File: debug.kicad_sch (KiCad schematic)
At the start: 47 parts, among them J701 USB4105-GF-A, J702 Conn_02x10_Odd_Even, U701 USBLC6-2SC6, U702 FT231XQ-R, U703 TCA9554PW

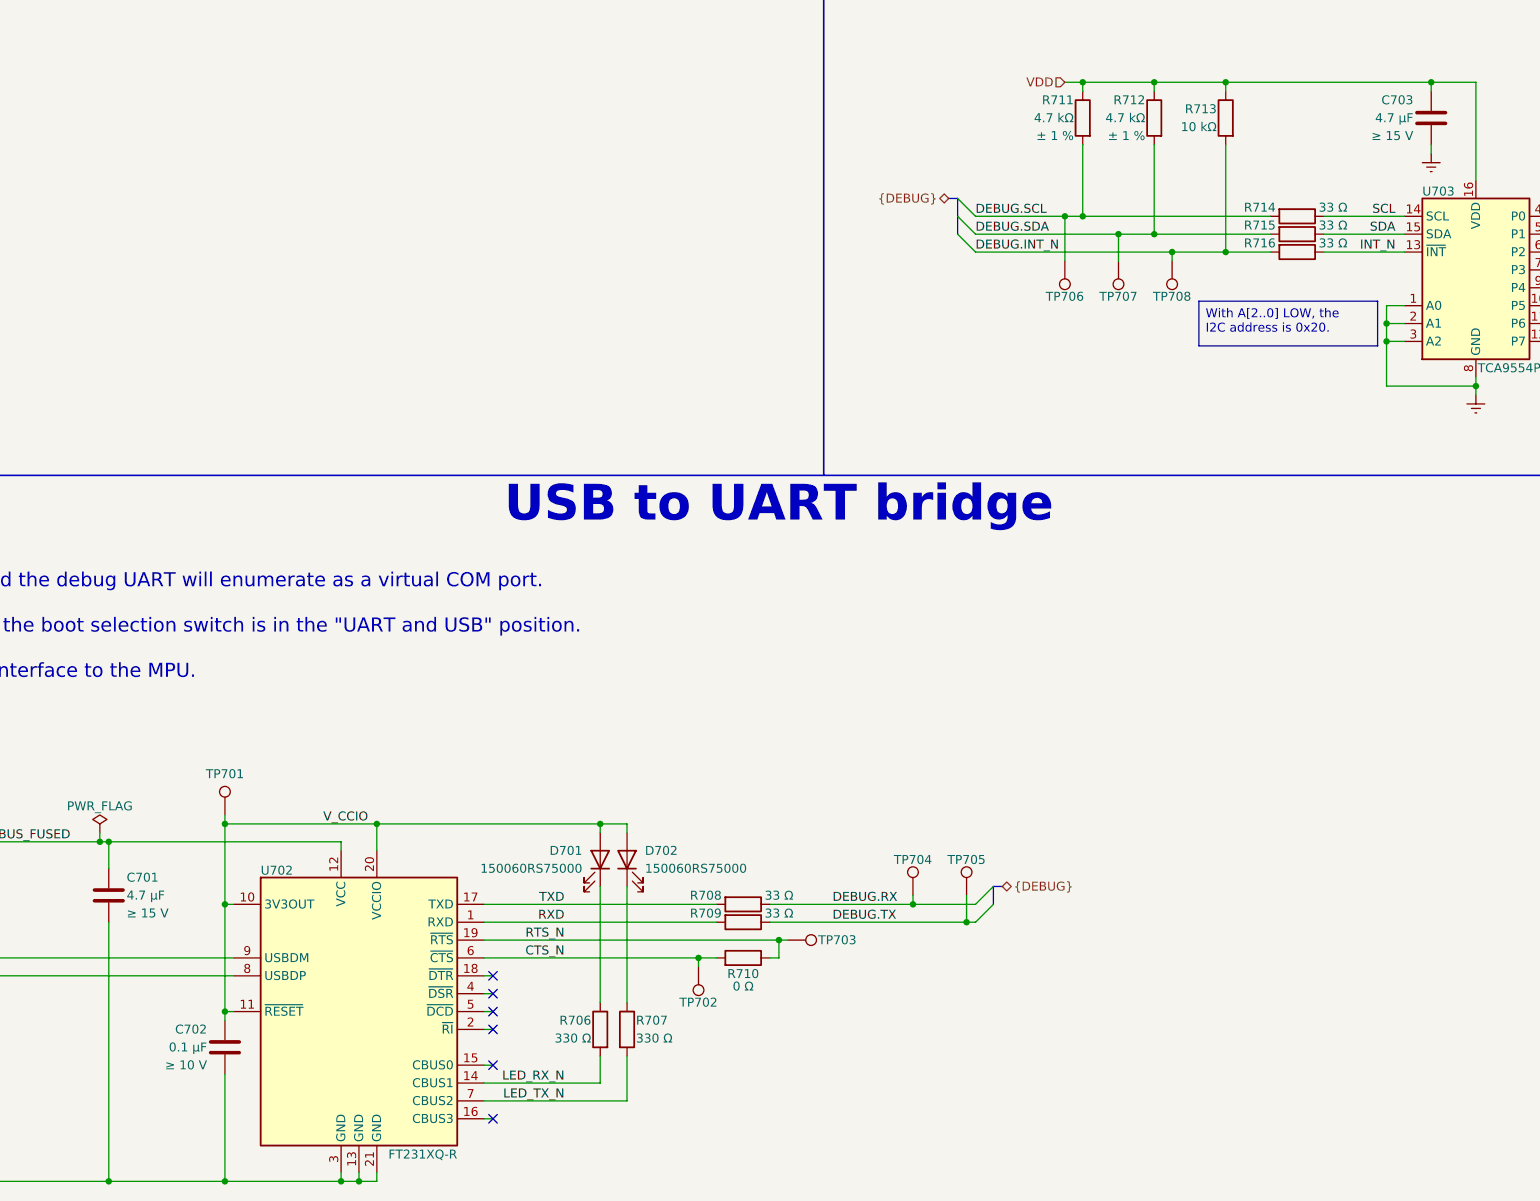
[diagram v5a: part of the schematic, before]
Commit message: Fix component values
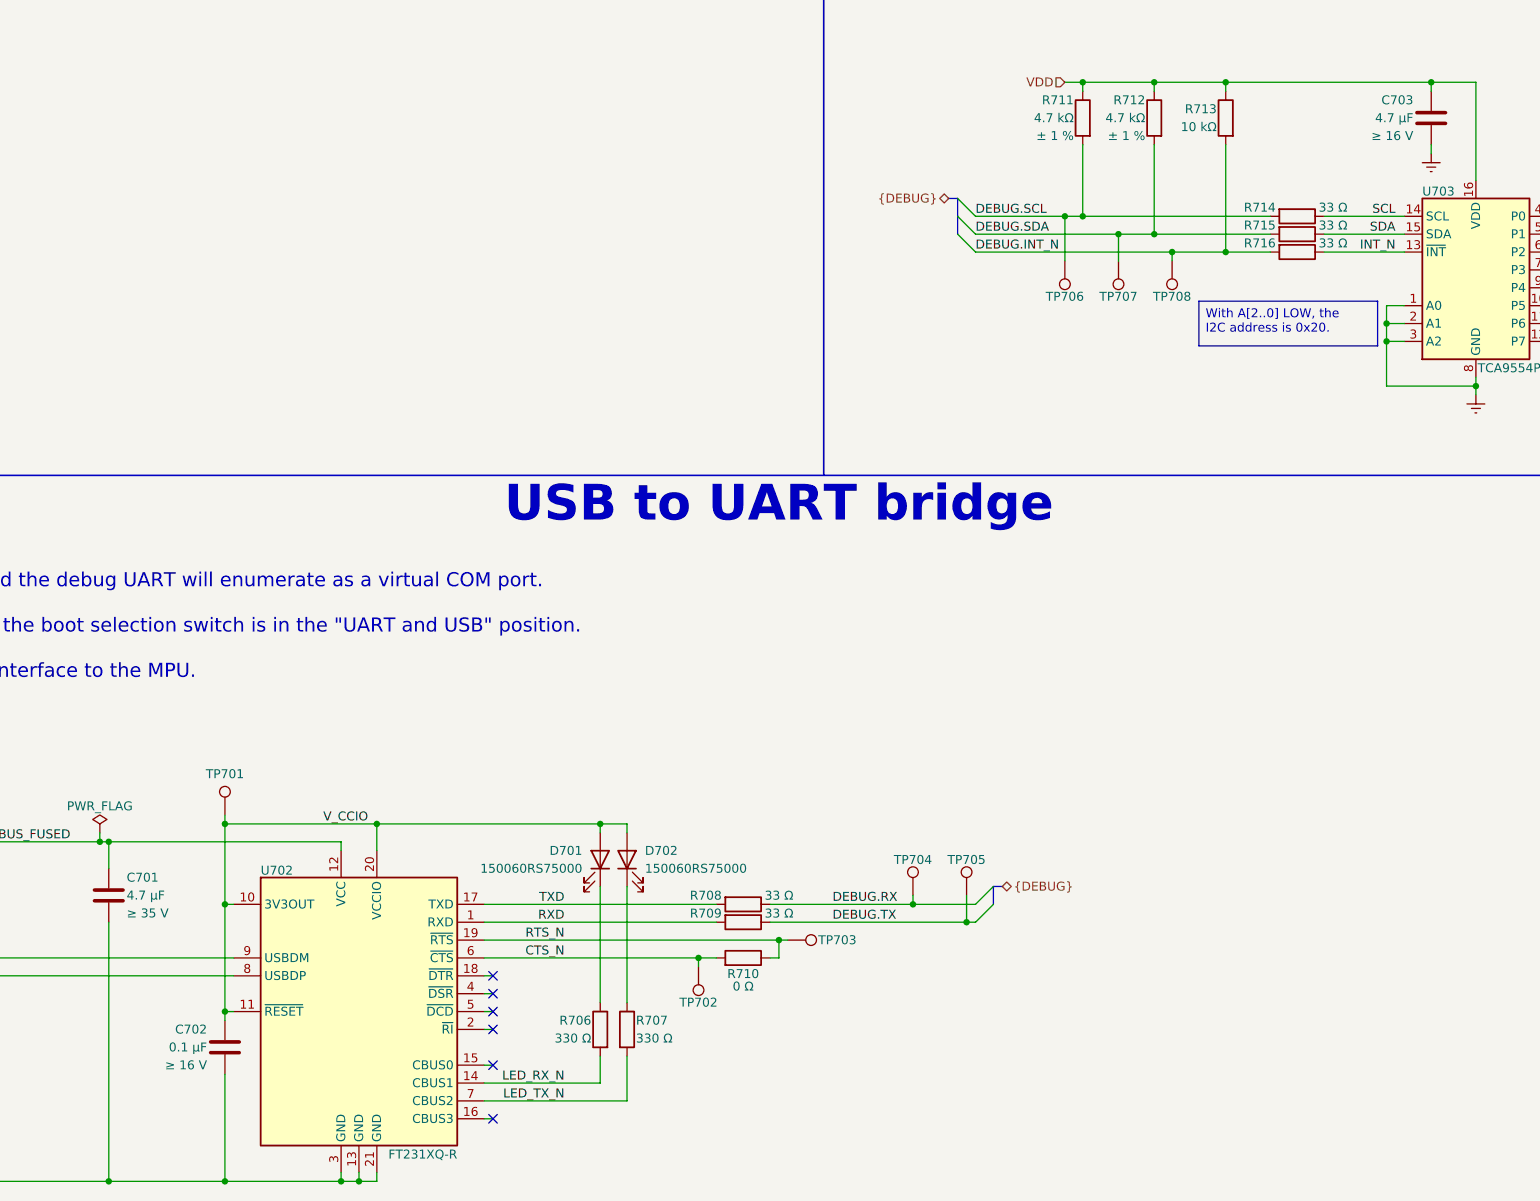
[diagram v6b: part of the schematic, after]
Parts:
- C701: Voltage rating ≥ 15 V -> ≥ 35 V
- C702: Voltage rating ≥ 10 V -> ≥ 16 V
- C703: Voltage rating ≥ 15 V -> ≥ 16 V
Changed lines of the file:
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@@
 			)
 		)
-		(property "Voltage rating" "≥ 15 V"
+		(property "Voltage rating" "≥ 16 V"
 			(at 299.72 88.9001 0)
 			(effects
@@
 			)
 		)
-		(property "Voltage rating" "≥ 10 V"
+		(property "Voltage rating" "≥ 16 V"
 			(at 128.27 220.9801 0)
 			(effects
@@
 			)
 		)
-		(property "Voltage rating" "≥ 15 V"
+		(property "Voltage rating" "≥ 35 V"
 			(at 116.84 199.3901 0)
 			(effects

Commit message: Refactor schematics
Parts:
- removed D703: 150141M173100, LED_SMD:LED_RGB_Wuerth-PLCC4_3.2x2.8mm_150141M173100, symbol Device:LED_ABRG
- removed R718, R721: 620 Ω, perfect_footprints:R_0402_1005Metric, symbol Device:R
- added C701: 0.01 µF, symbol Device:C
- added C703, C704: 47 pF, symbol Device:C
- added C705: 0.1 µF, symbol Device:C
- added D706: 150141M173100, LED_SMD:LED_RGB_Wuerth-PLCC4_3.2x2.8mm_150141M173100, symbol Device:LED_ABRG
- added FB701: ≥40 Ω @ 100 MHz, symbol Device:FerriteBead
- added R706, R707: 33 Ω, perfect_footprints:R_0402_1005Metric, symbol Device:R
- added R720, R723, R727, R728, R729, R730: 330 Ω, perfect_footprints:R_0402_1005Metric, symbol Device:R
- added TP701, TP702: TestPoint, TestPoint:TestPoint_Pad_D1.0mm, symbol Connector:TestPoint
- R719, R722: value 620 Ω -> 330 Ω; MPN 560112110020 -> 560112110019
- renumbered C701 to C702, C702 to C706, C703 to C707, D705 to D703, D706 to D704, D704 to D705, R711 to R708, R712 to R709, R713 to R710, R714 to R711, R715 to R712, R716 to R713, R706 to R714, R707 to R715, R717 to R716, R723 to R717, R720 to R718, R724 to R721, R708 to R724, R709 to R725, R710 to R726, TP706 to TP703, TP707 to TP704, TP701 to TP705, TP708 to TP706, TP702 to TP707, TP703 to TP708, TP704 to TP709, TP705 to TP710
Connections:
- net D_N: now also C704.1, R706.2; no longer U702.9 (USBDM)
- net D_P: now also C703.1, R707.2; no longer U702.8 (USBDP)
- net GND: now also C701.2, C703.2, C704.2, C705.2
- net LED3_K: now also R716.2, U703.4 (P0); no longer R717.2, U703.11 (P6)
- net LED4_K: now also R717.2, U703.5 (P1); no longer R721.2, U703.12 (P7)
- net RGB1_B: now also U703.9 (P4), R720.2; no longer R719.2, U703.6 (P2)
- net RGB1_G: now also R719.2, U703.7 (P3); no longer U703.5 (P1)
- net RGB1_R: now also R718.2, U703.6 (P2); no longer R716.2, U703.4 (P0)
- net RGB2_B: now also U703.12 (P7), R723.2; no longer R722.2, U703.10 (P5)
- net RGB2_G: now also R722.2, U703.11 (P6); no longer U703.9 (P4)
- net RGB2_R: now also R721.2, U703.10 (P5); no longer R718.2, U703.7 (P3)
- net V_5V0: now also D706.1 (A)
- net V_BUS: now also TP701.1
- net V_BUS_FUSED: now also C701.1, FB701.2; no longer C702.1, U702.12 (VCC)
- net at R722.1: now also R729.2; no longer D705.2 (BK)
- net at R716.1: now also D703.1 (K)
- net at D705.4 (GK): now also R727.1
- net at R717.1: now also D704.1 (K); no longer D703.1 (K)
- net at R719.1: now also R727.2
- net at R721.1: now also D706.3 (RK); no longer D704.1 (K)
- new net: D706.4 (GK), R729.1
- new net: D705.2 (BK), R728.1
- new net: D706.2 (BK), R730.1
- new net: R723.1, R730.2
- new net: R720.1, R728.2
- new net USBDM: R706.1, U702.9 (USBDM)
- new net USBDP: R707.1, U702.8 (USBDP)
- new net V_BUS_FILTERED: C702.1, C705.1, FB701.1, TP702.1, U702.12 (VCC)
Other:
- moved on the sheet: C702, C706, C707, D701, D702, D703, D704, D705, F701, J701, R703, R705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

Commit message: Clean-up schematics
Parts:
- added C701: 10 µF, Capacitor_SMD:C_0603_1608Metric, symbol Device:C
- R711, R712, R713, R724, R725: value 33 Ω -> 0 Ω
- renumbered C701 to C702, C702 to C703, C703 to C704, C704 to C705, C705 to C706, C706 to C707, C707 to C708
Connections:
- net GND: now also C701.2
- net VDD: now also C701.1
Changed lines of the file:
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@@
 	)
 	(junction
+		(at 96.52 128.27)
+		(diameter 0)
+		(color 0 0 0 0)
+	)
+	(junction
 		(at 187.96 102.87)
 		(diameter 0)
@@
 	)
 	(junction
+		(at 101.6 88.9)
+		(diameter 0)
+		(color 0 0 0 0)
+	)
+	(junction
 		(at 193.04 102.87)
 		(diameter 0)
@@
 	(wire
 		(pts
-			(xy 91.44 83.82) (xy 91.44 88.9)
+			(xy 101.6 83.82) (xy 101.6 88.9)
 		)
 		(stroke
@@
 	(wire
 		(pts
-			(xy 90.17 88.9) (xy 91.44 88.9)
+			(xy 90.17 88.9) (xy 101.6 88.9)
 		)
 		(stroke
@@
 	(wire
 		(pts
+			(xy 101.6 97.79) (xy 101.6 128.27)
+		)
+		(stroke
+			(width 0)
+			(type default)
+		)
+	)
+	(wire
+		(pts
 			(xy 165.1 189.23) (xy 165.1 190.5)
 		)
@@
 	(wire
 		(pts
-			(xy 76.2 83.82) (xy 91.44 83.82)
+			(xy 76.2 83.82) (xy 101.6 83.82)
 		)
 		(stroke
@@
 	(wire
 		(pts
+			(xy 101.6 88.9) (xy 101.6 90.17)
+		)
+		(stroke
+			(width 0)
+			(type default)
+		)
+	)
+	(wire
+		(pts
 			(xy 96.52 96.52) (xy 96.52 99.06)
 		)
@@
 	(wire
 		(pts
+			(xy 101.6 128.27) (xy 96.52 128.27)
+		)
+		(stroke
+			(width 0)
+			(type default)
+		)
+	)
+	(wire
+		(pts
 			(xy 354.33 118.11) (xy 354.33 86.36)
 		)
@@
 		(on_board yes)
 		(dnp no)
-		(property "Reference" "C701"
+		(property "Reference" "C702"
 			(at 111.76 218.44 0)
 			(effects
@@
 			(project "linux-sbc"
 				(path "/fa11a02f-8043-4153-ab69-88d766503017/5e32b227-0684-45b9-8c92-9550e4036164"
-					(reference "C701")
+					(reference "C702")
 					(unit 1)
 				)
@@
 		(on_board yes)
 		(dnp no)
-		(property "Reference" "C707"
+		(property "Reference" "C708"
 			(at 229.87 83.82 0)
 			(effects
@@
 			(project "linux-sbc"
 				(path "/fa11a02f-8043-4153-ab69-88d766503017/5e32b227-0684-45b9-8c92-9550e4036164"
-					(reference "C707")
+					(reference "C708")
 					(unit 1)
 				)
@@
 			)
 		)
-		(property "Value" "33 Ω"
+		(property "Value" "0 Ω"
 			(at 216.408 104.902 90)
 			(effects
@@
 		(on_board yes)
 		(dnp no)
-		(property "Reference" "C705"
+		(property "Reference" "C706"
 			(at 175.26 217.17 0)
 			(effects
@@
 			(project "linux-sbc"
 				(path "/fa11a02f-8043-4153-ab69-88d766503017/5e32b227-0684-45b9-8c92-9550e4036164"
-					(reference "C705")
+					(reference "C706")
 					(unit 1)
 				)
@@
 		(on_board yes)
 		(dnp no)
-		(property "Reference" "C706"
+		(property "Reference" "C707"
 			(at 187.96 217.17 0)
 			(effects
@@
 			(project "linux-sbc"
 				(path "/fa11a02f-8043-4153-ab69-88d766503017/5e32b227-0684-45b9-8c92-9550e4036164"
-					(reference "C706")
+					(reference "C707")
 					(unit 1)
 				)
@@
 			)
 		)
-		(property "Value" "33 Ω"
+		(property "Value" "0 Ω"
 			(at 216.408 99.822 90)
 			(effects
@@
 			)
 		)
-		(property "Value" "33 Ω"
+		(property "Value" "0 Ω"
 			(at 216.408 102.362 90)
 			(effects
@@
 	)
 	(symbol
+		(lib_id "Device:C")
+		(at 101.6 93.98 0)
+		(unit 1)
+		(exclude_from_sim no)
+		(in_bom yes)
+		(on_board yes)
+		(dnp no)
+		(property "Reference" "C701"
+			(at 104.14 91.44 0)
+			(effects
+				(font
+					(size 1.27 1.27)
+				)
+				(justify left)
+			)
+		)
+		(property "Value" "10 µF"
+			(at 104.14 93.98 0)
+			(effects
+				(font
+					(size 1.27 1.27)
+				)
+				(justify left)
+			)
+		)
+		(property "Footprint" "Capacitor_SMD:C_0603_1608Metric"
+			(at 102.5652 97.79 0)
+			(effects
+				(font
+					(size 1.27 1.27)
+				)
+				(hide yes)
+			)
+		)
+		(property "Datasheet" "https://search.murata.co.jp/Ceramy/image/img/A01X/G101/ENG/GRM188R6YA106MA73-01A.pdf"
+			(at 101.6 93.98 0)
+			(effects
+				(font
+					(size 1.27 1.27)
+				)
+				(hide yes)
+			)
+		)
+		(property "Description" "10 µF ±20% 35V Ceramic Capacitor X5R 0603 (1608 Metric)"
+			(at 101.6 93.98 0)
+			(effects
+				(font
+					(size 1.27 1.27)
+				)
+				(hide yes)
+			)
+		)
+		(property "MPN" "GRM188R6YA106MA73D"
+			(at 101.6 93.98 0)
+			(effects
+				(font
+					(size 1.27 1.27)
+				)
+				(hide yes)
+			)
+		)
+		(property "Manufacturer" "Murata Electronics"
+			(at 101.6 93.98 0)
+			(effects
+				(font
+					(size 1.27 1.27)
+				)
+				(hide yes)
+			)
+		)
+		(property "Voltage rating" "≥ 35 V"
+			(at 104.14 96.5201 0)
+			(effects
+				(font
+					(size 1.27 1.27)
+				)
+				(justify left)
+			)
+		)
+		(pin "2"
+		)
+		(pin "1"
+		)
+		(instances
+			(project "linux-sbc"
+				(path "/fa11a02f-8043-4153-ab69-88d766503017/5e32b227-0684-45b9-8c92-9550e4036164"
+					(reference "C701")
+					(unit 1)
+				)
+			)
+		)
+	)
+	(symbol
 		(lib_id "Device:R")
 		(at 276.86 199.39 270)
@@
 			)
 		)
-		(property "Value" "33 Ω"
+		(property "Value" "0 Ω"
 			(at 279.908 198.882 90)
 			(effects
@@
 		(on_board yes)
 		(dnp no)
-		(property "Reference" "C703"
+		(property "Reference" "C704"
 			(at 142.24 218.44 0)
 			(effects
@@
 			(project "linux-sbc"
 				(path "/fa11a02f-8043-4153-ab69-88d766503017/5e32b227-0684-45b9-8c92-9550e4036164"
-					(reference "C703")
+					(reference "C704")
 					(unit 1)
 				)
@@
 		(on_board yes)
 		(dnp no)
-		(property "Reference" "C704"
+		(property "Reference" "C705"
 			(at 154.94 218.44 0)
 			(effects
@@
 			(project "linux-sbc"
 				(path "/fa11a02f-8043-4153-ab69-88d766503017/5e32b227-0684-45b9-8c92-9550e4036164"
-					(reference "C704")
+					(reference "C705")
 					(unit 1)
 				)
@@
 		(on_board yes)
 		(dnp no)
-		(property "Reference" "C702"
+		(property "Reference" "C703"
 			(at 129.54 218.44 0)
 			(effects
@@
 			(project "linux-sbc"
 				(path "/fa11a02f-8043-4153-ab69-88d766503017/5e32b227-0684-45b9-8c92-9550e4036164"
-					(reference "C702")
+					(reference "C703")
 					(unit 1)
 				)
@@
 			)
 		)
-		(property "Value" "33 Ω"
+		(property "Value" "0 Ω"
 			(at 279.908 201.422 90)
 			(effects
